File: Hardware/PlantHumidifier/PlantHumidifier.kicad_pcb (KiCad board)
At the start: 2 copper layers, 66.8 x 57.9 mm, 12 parts, among them J1 110990030, J2 Conn_01x05_Female, J3 Conn_01x04_Female, J4 Conn_01x04_Female, U1 WeMos_D1_mini

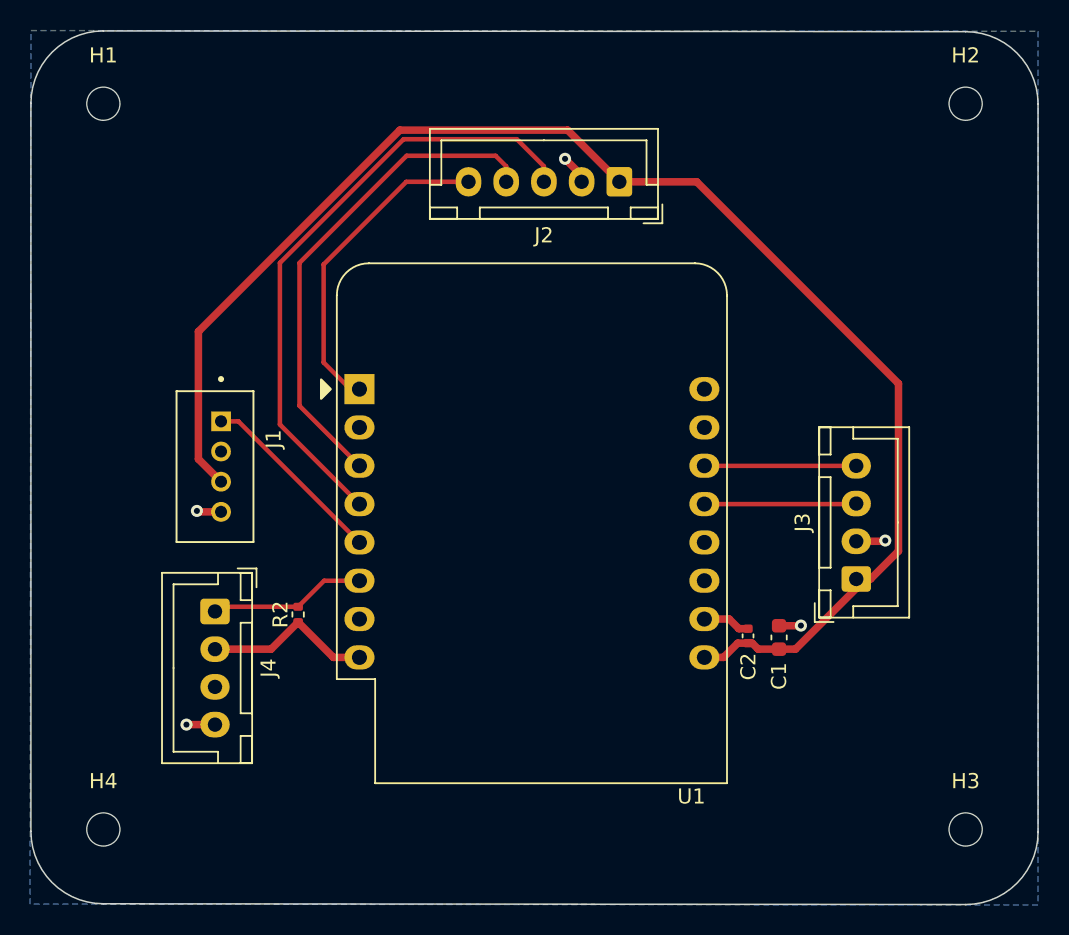
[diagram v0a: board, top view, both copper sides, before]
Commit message: Layout: Center Encoder
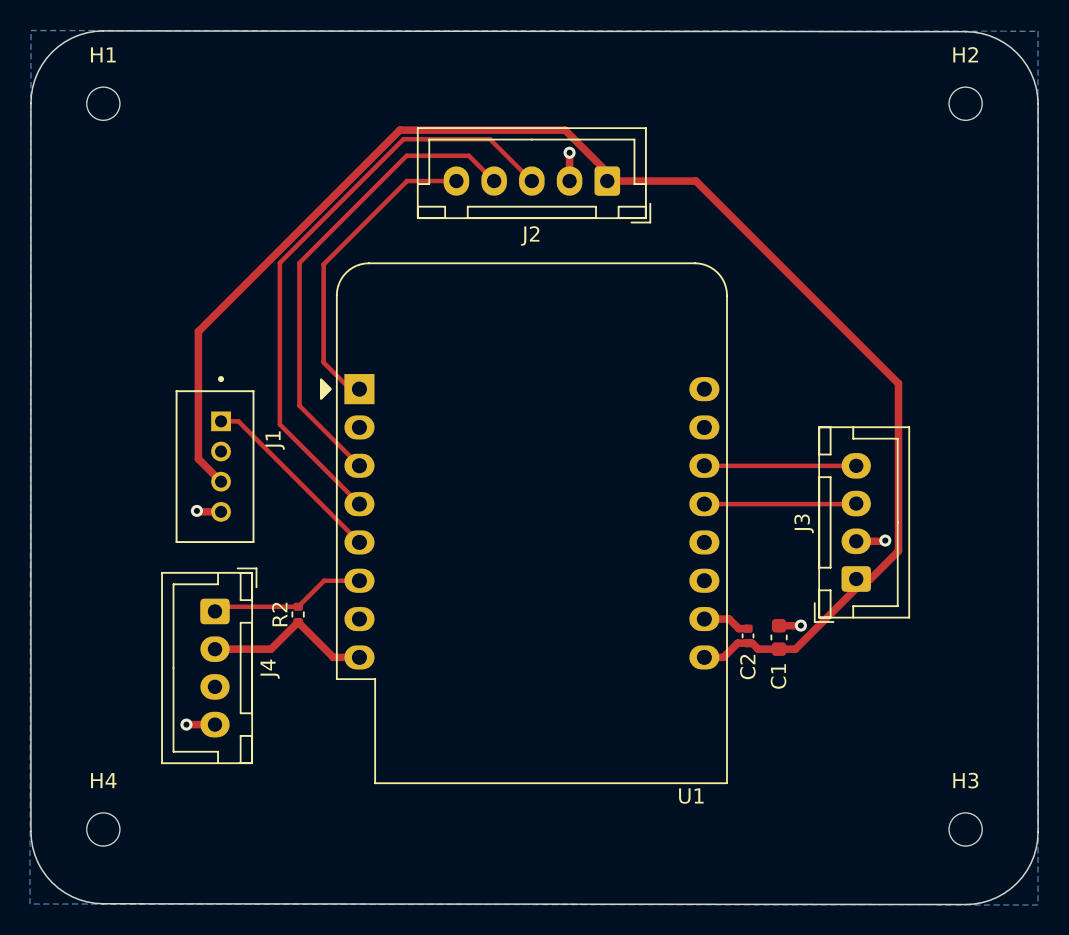
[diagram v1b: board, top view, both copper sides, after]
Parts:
- moved J2 0.80 mm to (94.0, 61.8)
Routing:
- net /Encoder_B: track 40.8 -> 39.4 mm
- net /Encoder_A: track 33.0 -> 31.6 mm
- net /Rst_n: track 21.5 -> 20.7 mm
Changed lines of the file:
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@@
   )
   (footprint "Connector_JST:JST_XH_B5B-XH-A_1x05_P2.50mm_Vertical" (layer "F.Cu")
-    (at 94.8 61.825 180)
+    (at 94 61.775 180)
     (descr "JST XH series connector, B5B-XH-A (http://www.jst-mfg.com/product/pdf/eng/eXH.pdf), generated with kicad-footprint-generator")
     (tags "connector JST XH vertical")
@@
   (gr_arc (start 117.75 51.875) (mid 121.144113 53.280887) (end 122.55 56.675) (layer "Edge.Cuts") (width 0.1))
   (segment (start 103.3272 92.4026) (end 103.604 92.4026) (width 0.5) (layer "F.Cu") (net 1))
+  (segment (start 99.875 61.775) (end 113.3 75.2) (width 0.5) (layer "F.Cu") (net 1))
   (segment (start 66.9 80.2) (end 66.9 71.751472) (width 0.5) (layer "F.Cu") (net 1))
   (segment (start 66.9 71.751472) (end 80.251472 58.4) (width 0.5) (layer "F.Cu") (net 1))
+  (segment (start 94 61.775) (end 99.875 61.775) (width 0.5) (layer "F.Cu") (net 1))
+  (segment (start 111.45 88.15) (end 110.5 88.15) (width 0.5) (layer "F.Cu") (net 1))
+  (segment (start 91.202082 58.4) (end 80.251472 58.4) (width 0.5) (layer "F.Cu") (net 1))
   (segment (start 106.472082 92.7992) (end 105.3846 92.7992) (width 0.5) (layer "F.Cu") (net 1))
   (segment (start 104.0006 92.7992) (end 105.3846 92.7992) (width 0.5) (layer "F.Cu") (net 1))
   (segment (start 103.604 92.4026) (end 104.0006 92.7992) (width 0.5) (layer "F.Cu") (net 1))
+  (segment (start 94 61.197918) (end 91.202082 58.4) (width 0.5) (layer "F.Cu") (net 1))
   (segment (start 102.644 92.4026) (end 103.3272 92.4026) (width 0.5) (layer "F.Cu") (net 1))
   (segment (start 68.4 81.7) (end 66.9 80.2) (width 0.5) (layer "F.Cu") (net 1))
-  (segment (start 113.3 86.3) (end 113.3 75.2) (width 0.5) (layer "F.Cu") (net 1))
-  (segment (start 94.8 61.825) (end 99.925 61.825) (width 0.5) (layer "F.Cu") (net 1))
-  (segment (start 80.251472 58.4) (end 91.375 58.4) (width 0.5) (layer "F.Cu") (net 1))
+  (segment (start 113.3 86.3) (end 111.45 88.15) (width 0.5) (layer "F.Cu") (net 1))
   (segment (start 110.5 88.771282) (end 106.472082 92.7992) (width 0.5) (layer "F.Cu") (net 1))
+  (segment (start 113.3 75.2) (end 113.3 86.3) (width 0.5) (layer "F.Cu") (net 1))
   (segment (start 101.7016 93.345) (end 102.644 92.4026) (width 0.5) (layer "F.Cu") (net 1))
-  (segment (start 113.3 75.2) (end 99.925 61.825) (width 0.5) (layer "F.Cu") (net 1))
-  (segment (start 91.375 58.4) (end 94.8 61.825) (width 0.5) (layer "F.Cu") (net 1))
-  (segment (start 111.45 88.15) (end 113.3 86.3) (width 0.5) (layer "F.Cu") (net 1))
-  (segment (start 110.5 88.15) (end 111.45 88.15) (width 0.5) (layer "F.Cu") (net 1))
+  (segment (start 94 61.775) (end 94 61.197918) (width 0.5) (layer "F.Cu") (net 1))
   (segment (start 110.5 88.15) (end 110.5 88.771282) (width 0.5) (layer "F.Cu") (net 1))
   (segment (start 100.434 93.345) (end 101.7016 93.345) (width 0.5) (layer "F.Cu") (net 1))
@@
   (segment (start 106.82 91.2492) (end 106.8324 91.2368) (width 0.5) (layer "F.Cu") (net 2))
   (segment (start 100.434 90.805) (end 102.0826 90.805) (width 0.5) (layer "F.Cu") (net 2))
+  (segment (start 91.5 61.775) (end 91.5 59.9) (width 0.5) (layer "F.Cu") (net 2))
   (segment (start 105.3846 91.2492) (end 106.82 91.2492) (width 0.5) (layer "F.Cu") (net 2))
   (segment (start 110.5 85.65) (end 112.375 85.65) (width 0.5) (layer "F.Cu") (net 2))
@@
   (segment (start 68.4 83.7) (end 66.8625 83.7) (width 0.5) (layer "F.Cu") (net 2))
   (segment (start 102.7202 91.4426) (end 103.3272 91.4426) (width 0.5) (layer "F.Cu") (net 2))
-  (segment (start 92.3 61.825) (end 92.3 61.4) (width 0.5) (layer "F.Cu") (net 2))
   (segment (start 112.375 85.65) (end 112.425 85.6) (width 0.5) (layer "F.Cu") (net 2))
-  (segment (start 92.3 61.4) (end 91.2 60.3) (width 0.5) (layer "F.Cu") (net 2))
   (via (at 66.8 83.6375) (size 0.8) (drill 0.4) (layers "F.Cu" "B.Cu") (net 2))
+  (via (at 91.5 59.9) (size 0.8) (drill 0.4) (layers "F.Cu" "B.Cu") (net 2))
   (via (at 66.1076 97.8) (size 0.8) (drill 0.4) (layers "F.Cu" "B.Cu") (net 2))
-  (via (at 91.2 60.3) (size 0.8) (drill 0.4) (layers "F.Cu" "B.Cu") (net 2))
   (via (at 106.8324 91.2368) (size 0.8) (drill 0.4) (layers "F.Cu" "B.Cu") (net 2))
   (via (at 112.425 85.6) (size 0.8) (drill 0.4) (layers "F.Cu" "B.Cu") (net 2))
@@
   (segment (start 72.3 77.911) (end 77.574 83.185) (width 0.3) (layer "F.Cu") (net 7))
   (segment (start 80.5 59) (end 72.3 67.2) (width 0.3) (layer "F.Cu") (net 7))
-  (segment (start 88 59) (end 80.5 59) (width 0.3) (layer "F.Cu") (net 7))
+  (segment (start 86.225 59) (end 80.5 59) (width 0.3) (layer "F.Cu") (net 7))
+  (segment (start 89 61.775) (end 86.225 59) (width 0.3) (layer "F.Cu") (net 7))
   (segment (start 72.3 67.2) (end 72.3 77.911) (width 0.3) (layer "F.Cu") (net 7))
-  (segment (start 89.8 60.8) (end 88 59) (width 0.3) (layer "F.Cu") (net 7))
-  (segment (start 89.8 61.825) (end 89.8 60.8) (width 0.3) (layer "F.Cu") (net 7))
+  (segment (start 86.5 61.775) (end 84.825 60.1) (width 0.3) (layer "F.Cu") (net 8))
   (segment (start 73.6 67.2) (end 73.6 76.671) (width 0.3) (layer "F.Cu") (net 8))
-  (segment (start 87.3 60.8) (end 86.6 60.1) (width 0.3) (layer "F.Cu") (net 8))
-  (segment (start 87.3 61.825) (end 87.3 60.8) (width 0.3) (layer "F.Cu") (net 8))
   (segment (start 73.6 76.671) (end 77.574 80.645) (width 0.3) (layer "F.Cu") (net 8))
   (segment (start 80.7 60.1) (end 73.6 67.2) (width 0.3) (layer "F.Cu") (net 8))
-  (segment (start 86.6 60.1) (end 80.7 60.1) (width 0.3) (layer "F.Cu") (net 8))
+  (segment (start 84.825 60.1) (end 80.7 60.1) (width 0.3) (layer "F.Cu") (net 8))
   (segment (start 68 92.8) (end 71.7176 92.8) (width 0.5) (layer "F.Cu") (net 10))
   (segment (start 73.5076 91.01) (end 75.8426 93.345) (width 0.5) (layer "F.Cu") (net 10))
@@
   (segment (start 75.2326 88.265) (end 77.574 88.265) (width 0.3) (layer "F.Cu") (net 11))
   (segment (start 73.5076 89.99) (end 68.31 89.99) (width 0.3) (layer "F.Cu") (net 11))
-  (segment (start 76.965 75.565) (end 77.574 75.565) (width 0.3) (layer "F.Cu") (net 14))
+  (segment (start 84 61.775) (end 80.725 61.775) (width 0.3) (layer "F.Cu") (net 14))
+  (segment (start 80.725 61.775) (end 75.2 67.3) (width 0.3) (layer "F.Cu") (net 14))
   (segment (start 75.2 73.8) (end 76.965 75.565) (width 0.3) (layer "F.Cu") (net 14))
   (segment (start 75.2 67.3) (end 75.2 73.8) (width 0.3) (layer "F.Cu") (net 14))
-  (segment (start 80.675 61.825) (end 75.2 67.3) (width 0.3) (layer "F.Cu") (net 14))
-  (segment (start 84.8 61.825) (end 80.675 61.825) (width 0.3) (layer "F.Cu") (net 14))
+  (segment (start 76.965 75.565) (end 77.574 75.565) (width 0.3) (layer "F.Cu") (net 14))
   (zone (net 2) (net_name "GND") (layer "B.Cu") (hatch edge 0.508)
     (connect_pads (clearance 0.3))
     (min_thickness 0.25) (filled_areas_thickness no)
-    (fill (thermal_gap 0.5) (thermal_bridge_width 0.5))
+    (fill yes (thermal_gap 0.5) (thermal_bridge_width 0.5))
     (polygon
       (pts

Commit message: Layout: Add silkscreen values, headers, & values
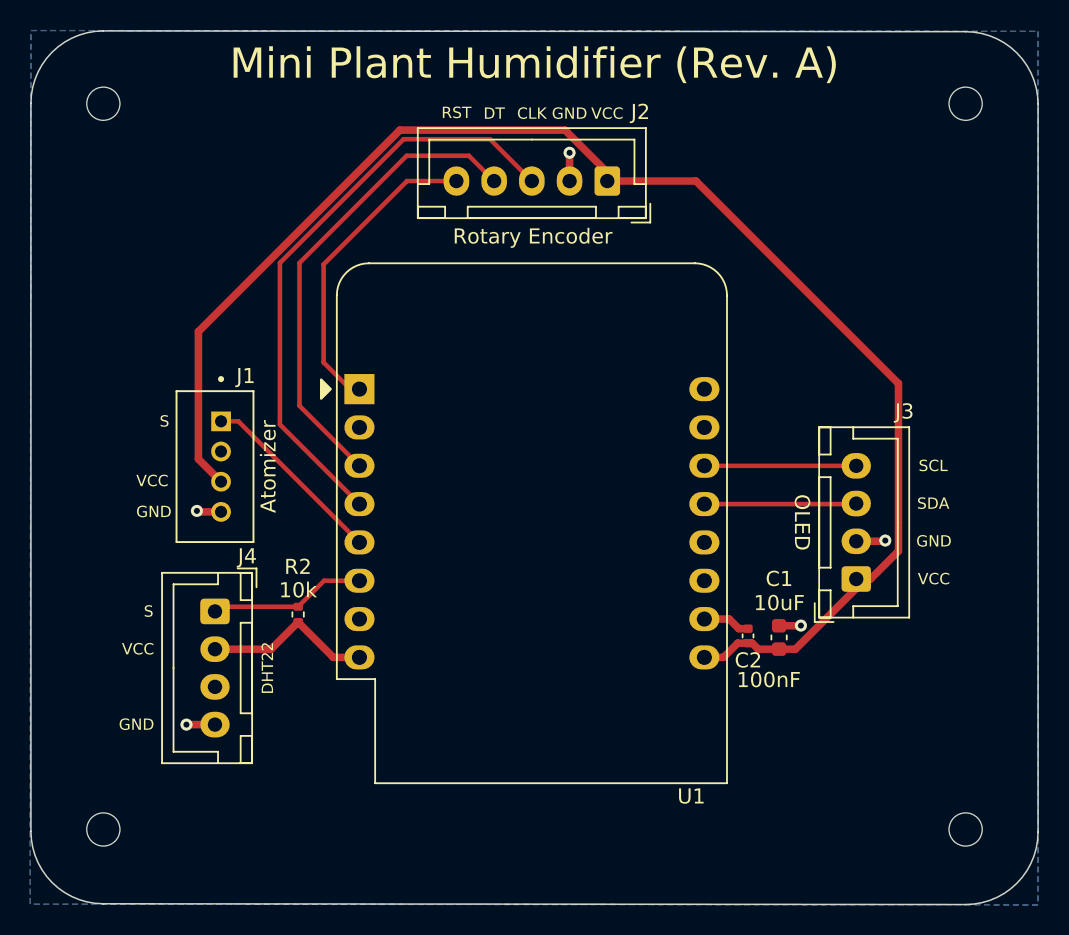
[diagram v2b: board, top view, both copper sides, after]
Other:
- board text added: "100nF"
- board text added: "10k"
- board text added: "10uF"
- board text added: "Atomizer"
- board text added: "CLK"
- board text added: "DHT22"
- board text added: "DT"
- board text added: "GND"
- board text added: "Mini Plant Humidifier (Rev. A)"
- board text added: "OLED"
- board text added: "RST"
- board text added: "Rotary Encoder"
- board text added: "S"
- board text added: "SCL"
- board text added: "SDA"
- board text added: "VCC"
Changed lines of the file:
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@@
     (property "Sheetname" "")
     (attr exclude_from_pos_files)
-    (fp_text reference "H4" (at 0 -3.2) (layer "F.SilkS")
+    (fp_text reference "H4" (at 0 -3.2) (layer "F.SilkS") hide
       (effects (font (size 1 1) (thickness 0.15)))
     )
@@
     (property "Sheetname" "")
     (attr through_hole)
-    (fp_text reference "J2" (at 5 -3.55) (layer "F.SilkS")
+    (fp_text reference "J2" (at -2.2 4.575) (layer "F.SilkS")
       (effects (font (size 1 1) (thickness 0.15)))
     )
@@
     (property "Sheetname" "")
     (attr smd)
-    (fp_text reference "C1" (at -2.5654 0 90) (layer "F.SilkS")
+    (fp_text reference "C1" (at 3.8742 0.0154) (layer "F.SilkS")
       (effects (font (size 1 1) (thickness 0.15)))
     )
@@
     (property "Sheetname" "")
     (attr smd)
-    (fp_text reference "C2" (at -2.032 0.0254 90) (layer "F.SilkS")
+    (fp_text reference "C2" (at -1.6274 0.0228 180) (layer "F.SilkS")
       (effects (font (size 1 1) (thickness 0.15)))
     )
@@
     (property "Sheetname" "")
     (attr through_hole)
-    (fp_text reference "J4" (at 3.75 -3.55 90) (layer "F.SilkS")
+    (fp_text reference "J4" (at -3.65 -2.15 180) (layer "F.SilkS")
       (effects (font (size 1 1) (thickness 0.15)))
     )
@@
     (property "Sheetname" "")
     (attr exclude_from_pos_files)
-    (fp_text reference "H3" (at 0 -3.2) (layer "F.SilkS")
+    (fp_text reference "H3" (at 0 -3.2) (layer "F.SilkS") hide
       (effects (font (size 1 1) (thickness 0.15)))
     )
@@
     (property "Sheetname" "")
     (attr smd)
-    (fp_text reference "R2" (at 0 -1.17 90) (layer "F.SilkS")
+    (fp_text reference "R2" (at 3.15 -0.0076 180) (layer "F.SilkS")
       (effects (font (size 1 1) (thickness 0.15)))
     )
@@
     (property "Sheetname" "")
     (attr through_hole)
-    (fp_text reference "J3" (at 3.75 -3.55 90) (layer "F.SilkS")
+    (fp_text reference "J3" (at 11.1 3.2 180) (layer "F.SilkS")
       (effects (font (size 1 1) (thickness 0.15)))
     )
@@
     (property "Sheetname" "")
     (attr exclude_from_pos_files)
-    (fp_text reference "H2" (at 0 -3.2) (layer "F.SilkS")
+    (fp_text reference "H2" (at 0 -3.2) (layer "F.SilkS") hide
       (effects (font (size 1 1) (thickness 0.15)))
     )
@@
     (property "Sheetname" "")
     (attr exclude_from_pos_files)
-    (fp_text reference "H1" (at 0 -3.2) (layer "F.SilkS")
+    (fp_text reference "H1" (at 0 -3.2) (layer "F.SilkS") hide
       (effects (font (size 1 1) (thickness 0.15)))
     )
@@
     (property "Sheetname" "")
     (attr through_hole)
-    (fp_text reference "J1" (at -1.825 -3.485 90) (layer "F.SilkS")
+    (fp_text reference "J1" (at -6 -1.65 180) (layer "F.SilkS")
       (effects (font (size 1 1) (thickness 0.15)))
     )
@@
   (gr_arc (start 60.6 109.675) (mid 57.205887 108.269113) (end 55.8 104.875) (layer "Edge.Cuts") (width 0.1))
   (gr_arc (start 117.75 51.875) (mid 121.144113 53.280887) (end 122.55 56.675) (layer "Edge.Cuts") (width 0.1))
+  (gr_text "VCC" (at 62.9 92.8) (layer "F.SilkS")
+    (effects (font (size 0.75 0.75) (thickness 0.15)))
+  )
+  (gr_text "GND" (at 62.8 97.8) (layer "F.SilkS")
+    (effects (font (size 0.75 0.75) (thickness 0.15)))
+  )
+  (gr_text "Mini Plant Humidifier (Rev. A)" (at 89.175 54) (layer "F.SilkS")
+    (effects (font (size 2 2) (thickness 0.3)))
+  )
+  (gr_text "RST" (at 84 57.25) (layer "F.SilkS")
+    (effects (font (size 0.75 0.75) (thickness 0.15)))
+  )
+  (gr_text "S" (at 63.6 90.3) (layer "F.SilkS")
+    (effects (font (size 0.75 0.75) (thickness 0.15)))
+  )
+  (gr_text "CLK" (at 89 57.3) (layer "F.SilkS")
+    (effects (font (size 0.75 0.75) (thickness 0.15)))
+  )
+  (gr_text "S" (at 64.65 77.7) (layer "F.SilkS")
+    (effects (font (size 0.75 0.75) (thickness 0.15)))
+  )
+  (gr_text "10uF" (at 105.4 89.75) (layer "F.SilkS")
+    (effects (font (size 1 1) (thickness 0.15)))
+  )
+  (gr_text "VCC" (at 63.85 81.65) (layer "F.SilkS")
+    (effects (font (size 0.75 0.75) (thickness 0.15)))
+  )
+  (gr_text "Rotary Encoder" (at 89.05 65.45) (layer "F.SilkS")
+    (effects (font (size 1 1) (thickness 0.15)))
+  )
+  (gr_text "SCL" (at 115.6 80.65) (layer "F.SilkS")
+    (effects (font (size 0.75 0.75) (thickness 0.15)))
+  )
+  (gr_text "OLED" (at 106.9 84.4 270) (layer "F.SilkS")
+    (effects (font (size 1 1) (thickness 0.15)))
+  )
+  (gr_text "VCC" (at 94 57.3) (layer "F.SilkS")
+    (effects (font (size 0.75 0.75) (thickness 0.15)))
+  )
+  (gr_text "GND" (at 115.65 85.65) (layer "F.SilkS")
+    (effects (font (size 0.75 0.75) (thickness 0.15)))
+  )
+  (gr_text "GND" (at 91.5 57.3) (layer "F.SilkS")
+    (effects (font (size 0.75 0.75) (thickness 0.15)))
+  )
+  (gr_text "DHT22" (at 71.5 94.05 90) (layer "F.SilkS")
+    (effects (font (size 0.75 0.75) (thickness 0.15)))
+  )
+  (gr_text "Atomizer" (at 71.55 80.7 90) (layer "F.SilkS")
+    (effects (font (size 1 1) (thickness 0.15)))
+  )
+  (gr_text "100nF" (at 104.7 94.85) (layer "F.SilkS")
+    (effects (font (size 1 1) (thickness 0.15)))
+  )
+  (gr_text "GND" (at 63.95 83.7) (layer "F.SilkS")
+    (effects (font (size 0.75 0.75) (thickness 0.15)))
+  )
+  (gr_text "10k" (at 73.5 88.9) (layer "F.SilkS")
+    (effects (font (size 1 1) (thickness 0.15)))
+  )
+  (gr_text "VCC" (at 115.65 88.15) (layer "F.SilkS")
+    (effects (font (size 0.75 0.75) (thickness 0.15)))
+  )
+  (gr_text "SDA" (at 115.6 83.15) (layer "F.SilkS")
+    (effects (font (size 0.75 0.75) (thickness 0.15)))
+  )
+  (gr_text "DT" (at 86.5 57.3) (layer "F.SilkS")
+    (effects (font (size 0.75 0.75) (thickness 0.15)))
+  )
   (segment (start 103.3272 92.4026) (end 103.604 92.4026) (width 0.5) (layer "F.Cu") (net 1))
   (segment (start 99.875 61.775) (end 113.3 75.2) (width 0.5) (layer "F.Cu") (net 1))
@@
     (connect_pads (clearance 0.3))
     (min_thickness 0.25) (filled_areas_thickness no)
-    (fill yes (thermal_gap 0.5) (thermal_bridge_width 0.5))
+    (fill (thermal_gap 0.5) (thermal_bridge_width 0.5))
     (polygon
       (pts

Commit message: Layout: Add silkscreen title and relevant information about design
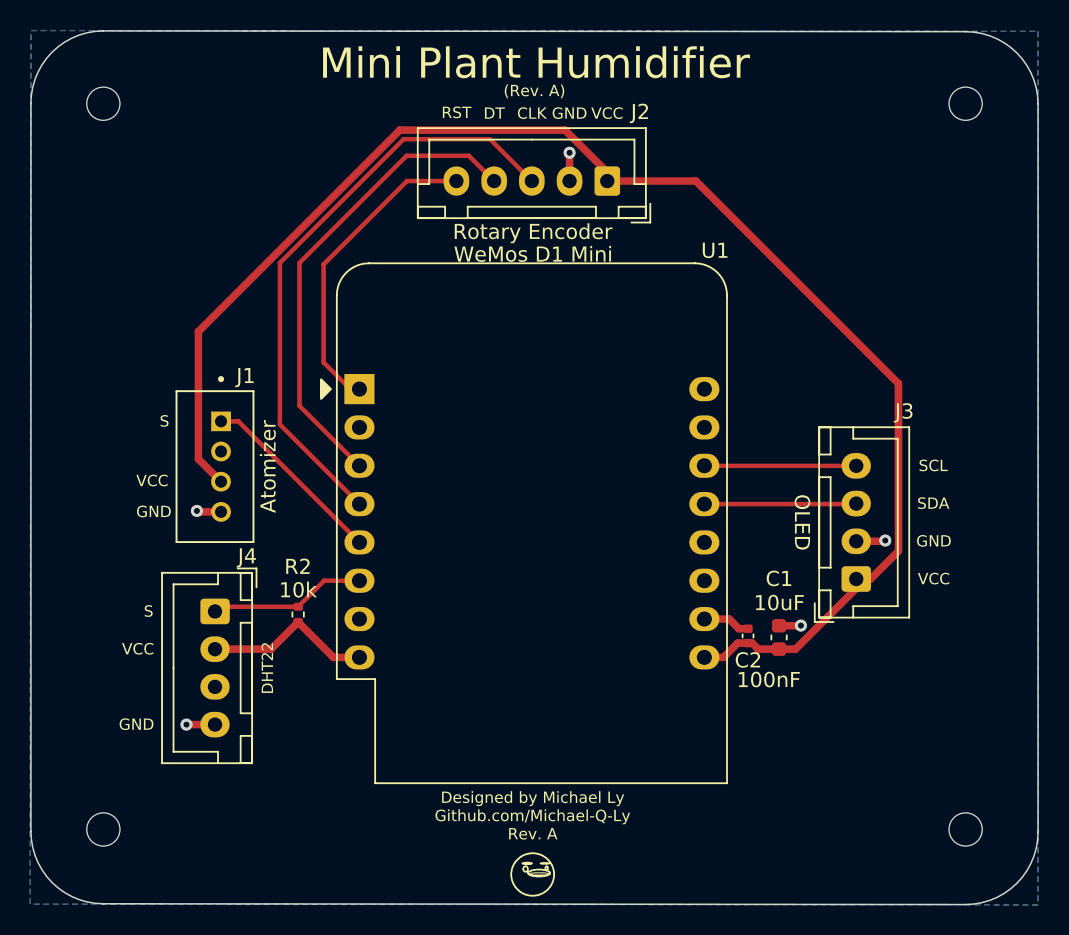
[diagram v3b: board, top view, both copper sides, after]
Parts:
- added G***: LOGO, Ducky:Ducky, F.Cu at (89.0, 107.8)
- added REF**: OSHW-Logo_5.7x6mm_SilkScreen, Symbol:OSHW-Logo_5.7x6mm_SilkScreen, B.Cu at (89.0, 91.3)
- added REF**: KiCad-Logo2_6mm_SilkScreen, Symbol:KiCad-Logo2_6mm_SilkScreen, B.Cu at (89.0, 77.3)
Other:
- board text added: "(Rev. A)"
- board text added: "Designed by Michael Ly Github.com/Michael-Q-Ly Rev. A"
- board text added: "Mini Plant Humidifier"
- board text added: "WeMos D1 Mini"
- board text removed: "Mini Plant Humidifier (Rev. A)"
